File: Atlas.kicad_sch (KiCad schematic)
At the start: 45 parts, among them J101 BATT, J102 GND, J103 A, J104 B, J105 C, J106 Conn_01x05, U102 LMR51420YDDCR, U103 TLV76733DRVR

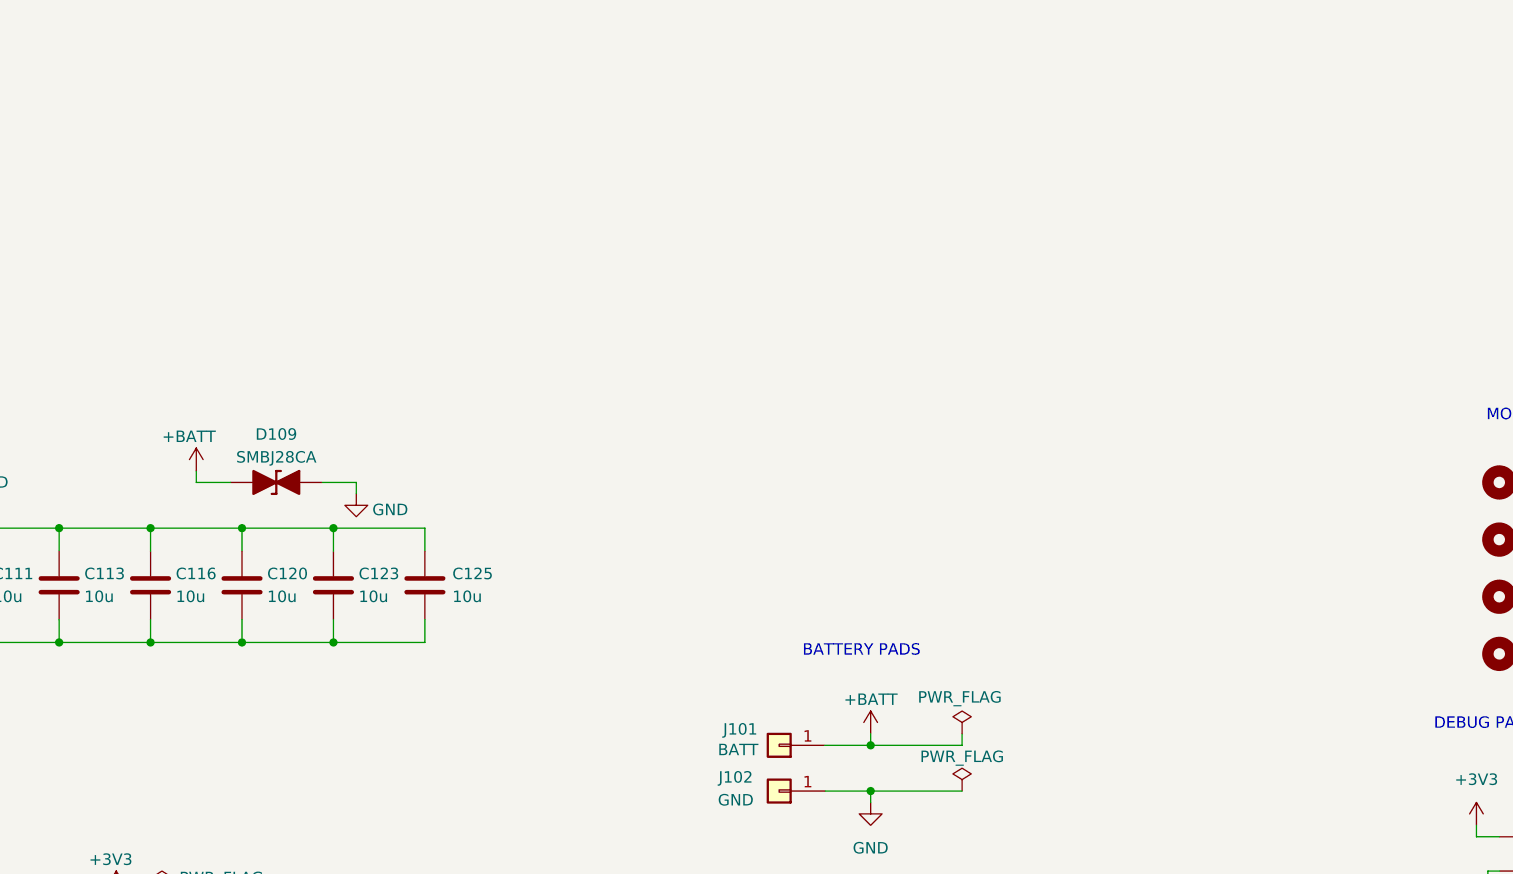
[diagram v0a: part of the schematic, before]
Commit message: esc design and current shunt resistor changes and parallel tvs diodes - still unfinished
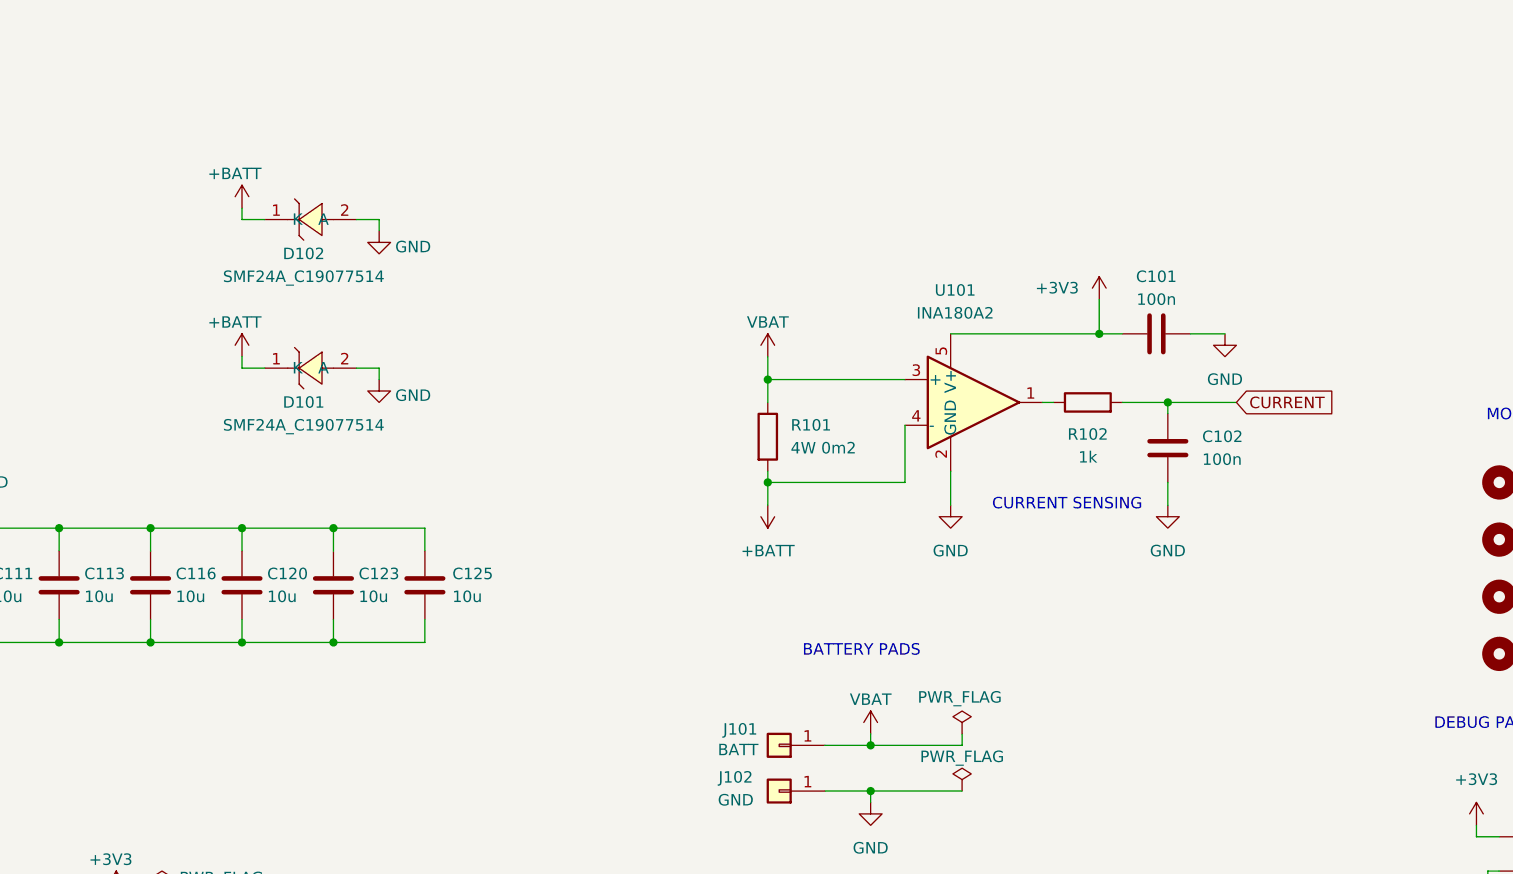
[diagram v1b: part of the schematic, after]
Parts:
- removed D109: SMBJ28CA, PCM_Diode_SMD_AKL:D_SMB_TVS, symbol PCM_Diode_TVS_AKL:SMBJ28CA
- added C101, C102: 100n, symbol Device:C
- added D101, D102: SMF24A_C19077514, easyeda2kicad:SOD-123FL_L2.7-W1.8-LS3.8-RD, symbol easyeda2kicad:SMF24A_C19077514
- added R101: 4W 0m2, symbol Device:R
- added R102: 1k, symbol Device:R
- added U101: INA180A2, Package_TO_SOT_SMD:SOT-23-5, symbol Amplifier_Current:INA180A2
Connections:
- net +3V3: now also C101.2, U101.5 (V+)
- net +BATT: now also D101.1 (K), D102.1 (K), R101.2, U101.4 (-); no longer J101.1 (Pin_1)
- net CURRENT: now also C102.1, R102.2
- net GND: now also C101.1, C102.2, D101.2 (A), D102.2 (A), U101.2 (GND)
- new net: R102.1, U101.1
- new net VBAT: J101.1 (Pin_1), R101.1, U101.3 (+)
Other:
- note added: "CURRENT SENSING"

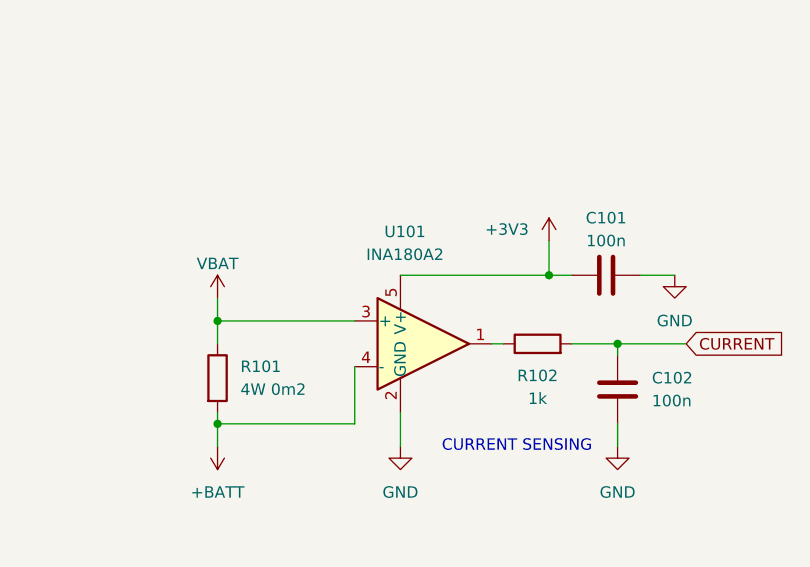
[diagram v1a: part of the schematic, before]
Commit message: switched ina current sense to ina186
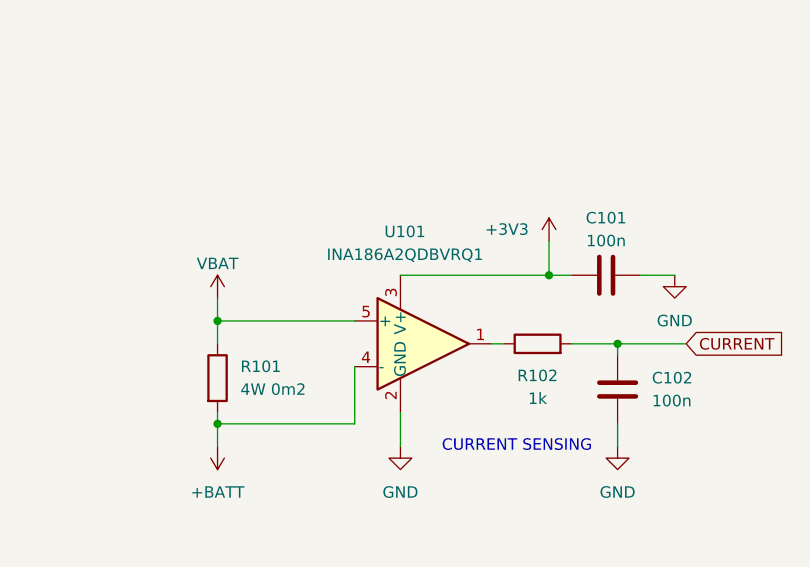
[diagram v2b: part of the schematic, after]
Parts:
- U101: value INA180A2 -> INA186A2QDBVRQ1; footprint Package_TO_SOT_SMD:SOT-23-5 -> 4in1ESC:SOT-23-5_L2.9-W1.6-P0.95-LS2.8-BR; symbol Amplifier_Current:INA180A2 -> TexasInstruments:INA186A2QDBVRQ1; MPN INA180A2IDBVR -> INA186A2QDBVRQ1; Manufacturer TI -> Texas Instruments; lcsc C192764 -> C2867989
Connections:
- net +3V3: now also U101.3 (V+); no longer U101.5 (V+)
- net VBAT: now also U101.5 (+); no longer U101.3 (+)
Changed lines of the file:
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@@
 	)
 	(symbol
-		(lib_id "Amplifier_Current:INA180A2")
+		(lib_id "TexasInstruments:INA186A2QDBVRQ1")
 		(at 176.53 50.8 0)
 		(unit 1)
@@
 			)
 		)
-		(property "Value" "INA180A2"
+		(property "Value" "INA186A2QDBVRQ1"
 			(at 174.498 40.894 0)
 			(show_name no)
@@
 			)
 		)
-		(property "Footprint" "Package_TO_SOT_SMD:SOT-23-5"
+		(property "Footprint" "4in1ESC:SOT-23-5_L2.9-W1.6-P0.95-LS2.8-BR"
 			(at 177.8 49.53 0)
 			(hide yes)
@@
 			)
 		)
-		(property "Datasheet" "https://datasheet.lcsc.com/datasheet/pdf/677f1f8d058cefecb8bbd499517bf8e1.pdf?productCode=C192764"
+		(property "Datasheet" "https://www.lcsc.com/datasheet/lcsc_datasheet_2302220000_Texas-Instruments-INA186A2QDBVRQ1_C2867989.pdf"
 			(at 180.34 46.99 0)
 			(hide yes)
@@
 			)
 		)
-		(property "Description" "Current Sense Amplifier, 1 Circuit, Rail-to-Rail, 26V, Gain 50 V/V, SOT-23-5"
+		(property "Description" "符合AEC-Q100标准且具有皮安级IB and 使能引脚的40V、双向、高精度电流感测放大器, SOT-23-5"
 			(at 176.53 50.8 0)
 			(hide yes)
@@
 			)
 		)
-		(property "Manufacturer" "TI"
+		(property "Manufacturer" "Texas Instruments"
 			(at 104.14 -129.54 0)
 			(hide yes)
@@
 			)
 		)
-		(property "MPN" "INA180A2IDBVR"
+		(property "MPN" "INA186A2QDBVRQ1"
 			(at 104.14 -129.54 0)
 			(hide yes)
@@
 			)
 		)
-		(property "lcsc" "C192764"
+		(property "lcsc" "C2867989"
 			(at 104.14 -129.54 0)
 			(hide yes)
